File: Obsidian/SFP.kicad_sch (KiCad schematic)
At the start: 82 parts, among them J1 TYCO_1888247-1, J11 TYCO_1888247-1, J12 TYCO_1888247-1, J13 TYCO_1888247-1, J8 2180739-1, J9 2180739-1, U17 TCA9555RTWR, U19 TCA9555RTWR, U26 PCA9546ARGV

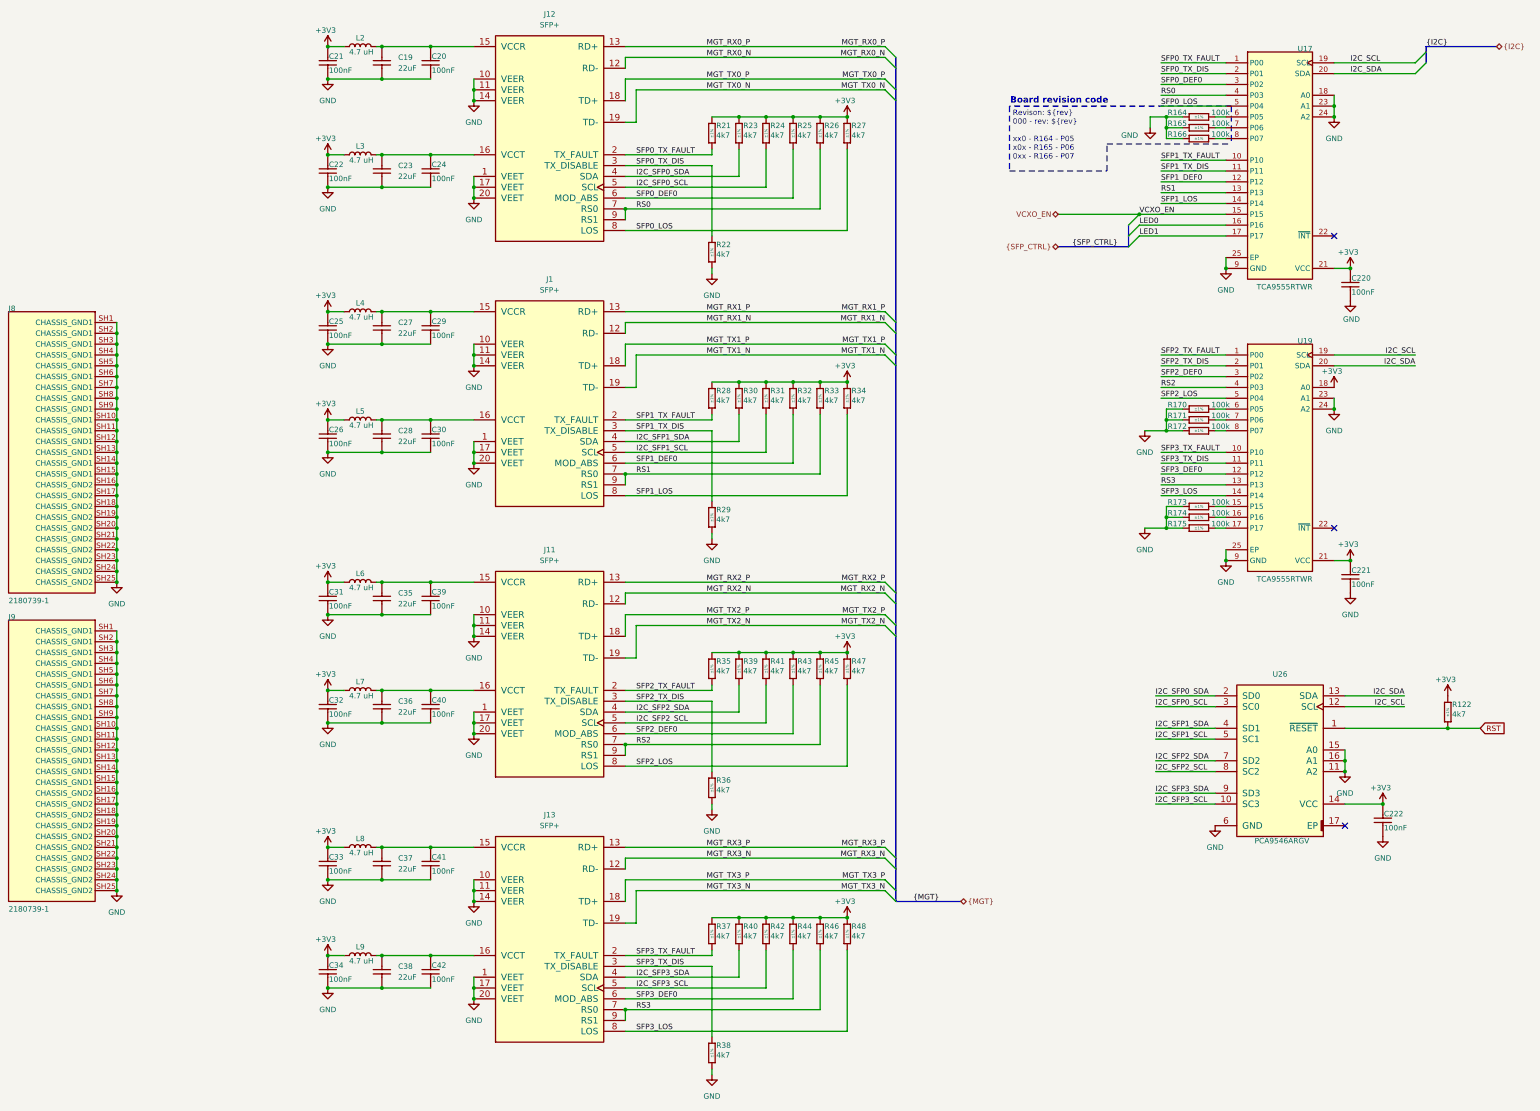
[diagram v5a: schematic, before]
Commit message: adding flex connector
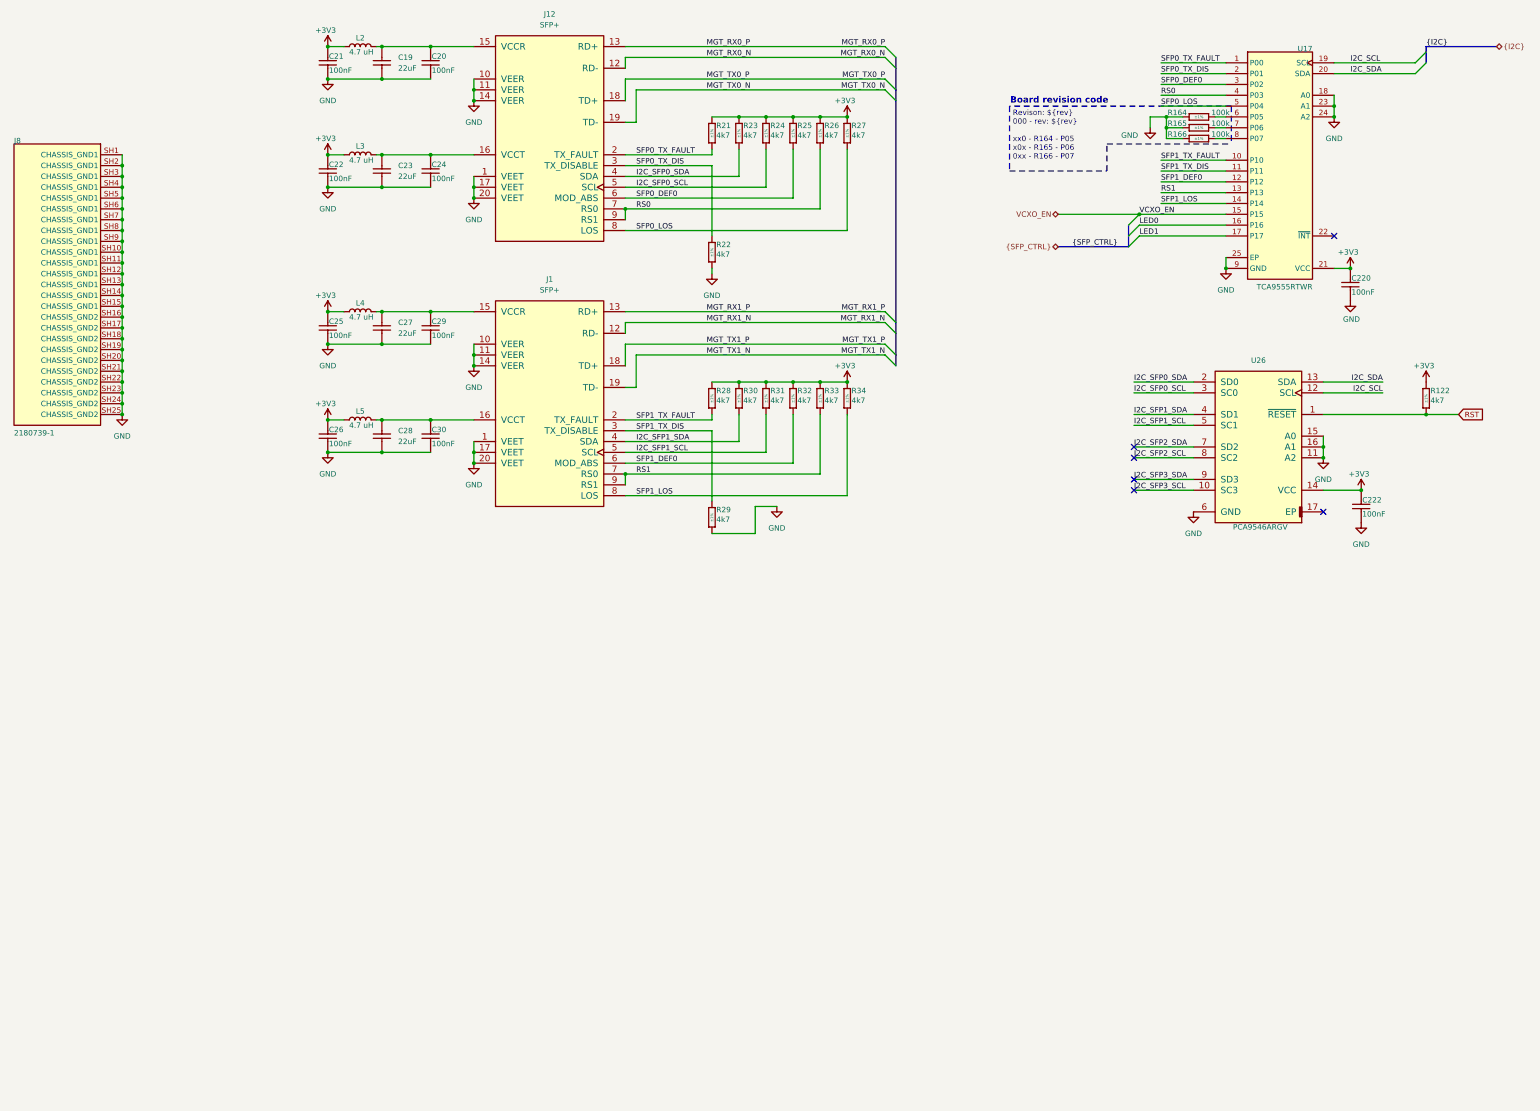
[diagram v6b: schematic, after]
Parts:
- removed C221, C31, C32, C33, C34, C39, C40, C41, C42: CC0402_100NF_50V_10%_X7R, Capacitor_SMD:C_0402_1005Metric, symbol Library_Symbol:CC0402_100NF_50V_10%_X7R
- removed C35, C36, C37, C38: CC0805_22UF_16V_10%_X5R, Footprint:CAPC2012X135N, symbol Library_Symbol:CC0805_22UF_16V_10%_X5R
- removed J11, J13: TYCO_1888247-1, Footprint:TYCO_1888247-1, symbol Library_Symbol:TYCO_1888247-1
- removed J9: 2180739-1, Footprint:TE_2180739-1, symbol Library_Symbol:root_0_2180739-1
- removed L6, L7, L8, L9: 4.7 uH, Footprint:L_1008_2520Metric, symbol Library_Symbol:L
- removed R170, R171, R172, R173, R174, R175: R0402_100K_1%_0.0625W_100PPM, Footprint:RESC1005X40N, symbol Library_Symbol:R0402_100K_1%_0.0625W_100PPM
- removed R35, R36, R37, R38, R39, R40, R41, R42, R43, R44, R45, R46, R47, R48: R0402_4K7_1%_0.0625W_100PPM, Footprint:RESC1005X40N, symbol Library_Symbol:R0402_4K7_1%_0.0625W_100PPM
- removed U19: TCA9555RTWR, Footprint:QFN50P400X400X80-25N-S245, symbol Library_Symbol:root_0_TI-TCA9535-QFN_RTW-24
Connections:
- no-connect marks 3 -> 6
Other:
- moved on the sheet: C222, J8, R122, U26

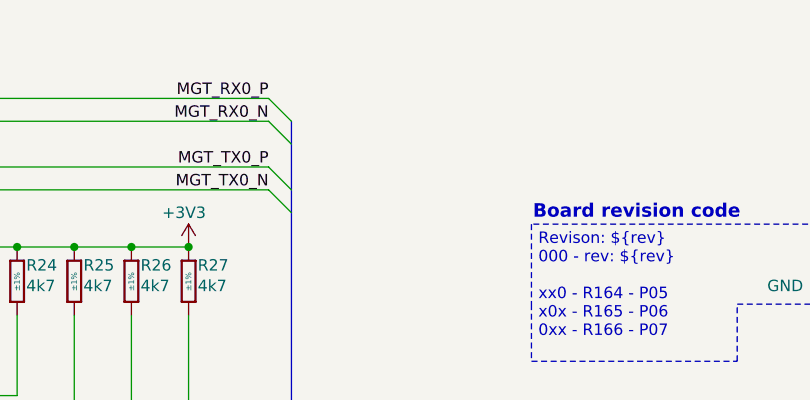
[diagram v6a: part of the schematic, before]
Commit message: Cleanup of the schematic
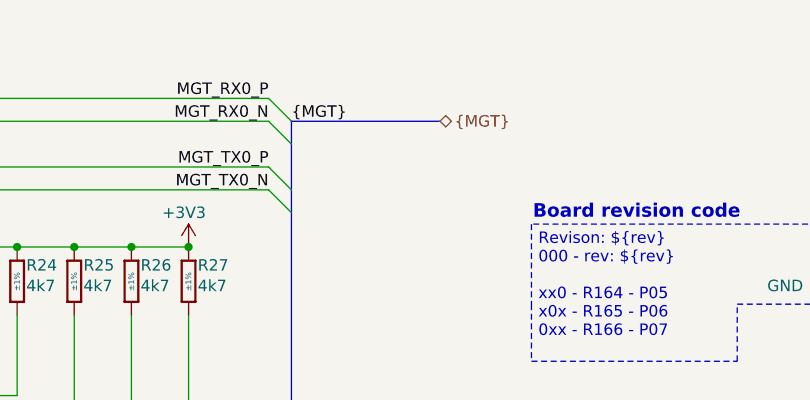
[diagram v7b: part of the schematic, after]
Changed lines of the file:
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@@
+		)
+	)
+	(bus
+		(pts
+			(xy 246.38 27.94) (xy 262.89 27.94)
+		)
+		(stroke
+			(width 0)
+			(type default)
 		)
 	)
@@
 				(size 1.27 1.27)
 				(thickness 0.1588)
+			)
+			(justify left bottom)
+		)
+	)
+	(label "{MGT}"
+		(at 246.38 27.94 0)
+		(effects
+			(font
+				(size 1.27 1.27)
 			)
 			(justify left bottom)
@@
 		)
 	)
+	(hierarchical_label "{MGT}"
+		(shape bidirectional)
+		(at 262.89 27.94 0)
+		(effects
+			(font
+				(size 1.27 1.27)
+			)
+			(justify left)
+		)
+	)

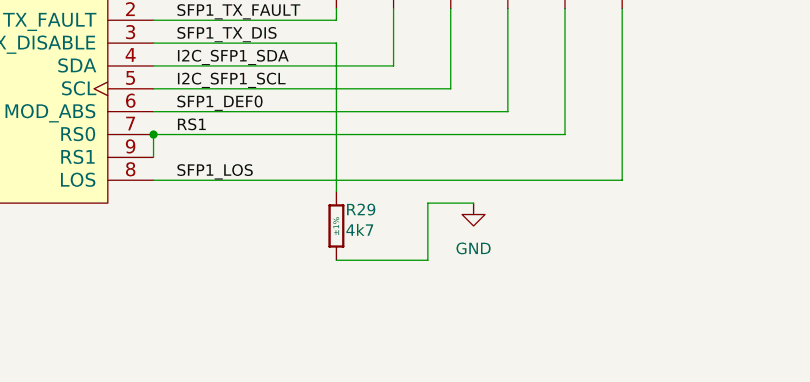
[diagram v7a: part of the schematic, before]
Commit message: correcting some footprint issues
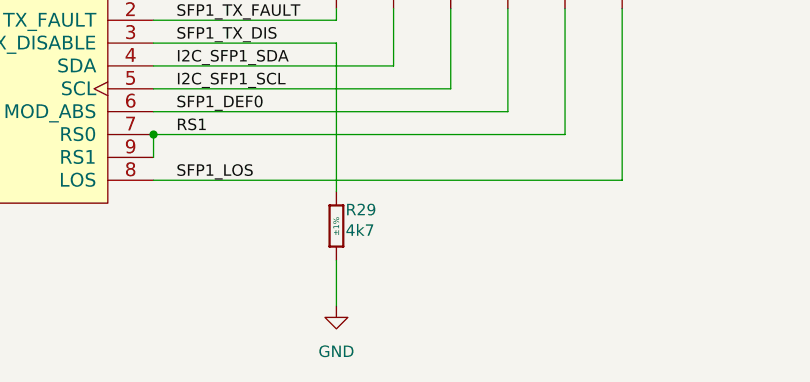
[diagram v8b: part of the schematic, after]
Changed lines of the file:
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@@
 	(wire
 		(pts
-			(xy 213.36 139.7) (xy 203.2 139.7)
-		)
-		(stroke
-			(width 0)
-			(type default)
-		)
-	)
-	(wire
-		(pts
 			(xy 303.53 64.77) (xy 323.85 64.77)
 		)
@@
 	(wire
 		(pts
-			(xy 213.36 139.7) (xy 213.36 133.35)
+			(xy 203.2 144.78) (xy 203.2 139.7)
 		)
 		(stroke
@@
 	(wire
 		(pts
-			(xy 213.36 133.35) (xy 218.44 133.35)
-		)
-		(stroke
-			(width 0)
-			(type default)
-		)
-	)
-	(wire
-		(pts
 			(xy 182.88 33.02) (xy 182.88 38.1)
 		)
@@
 	(symbol
 		(lib_id "Library_Symbol:GND")
-		(at 218.44 133.35 0)
+		(at 203.2 144.78 0)
 		(unit 1)
 		(exclude_from_sim no)
@@
 		(fields_autoplaced yes)
 		(property "Reference" "#PWR047"
-			(at 218.44 139.7 0)
+			(at 203.2 151.13 0)
 			(effects
 				(font
@@
 		)
 		(property "Value" "GND"
-			(at 218.44 138.43 0)
+			(at 203.2 149.86 0)
 			(effects
 				(font
@@
 		)
 		(property "Footprint" ""
-			(at 218.44 133.35 0)
+			(at 203.2 144.78 0)
 			(effects
 				(font
@@
 		)
 		(property "Datasheet" ""
-			(at 218.44 133.35 0)
+			(at 203.2 144.78 0)
 			(effects
 				(font
@@
 		)
 		(property "Description" "Power symbol creates a global label with name \"GND\" , ground"
-			(at 218.44 133.35 0)
+			(at 203.2 144.78 0)
 			(effects
 				(font
